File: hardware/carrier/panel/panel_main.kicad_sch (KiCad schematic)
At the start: 23 parts, among them J1 GDEY029T94 FPC, J2 CARRIER, J3 FRONTLIGHT FPC, Q5 AO3400A

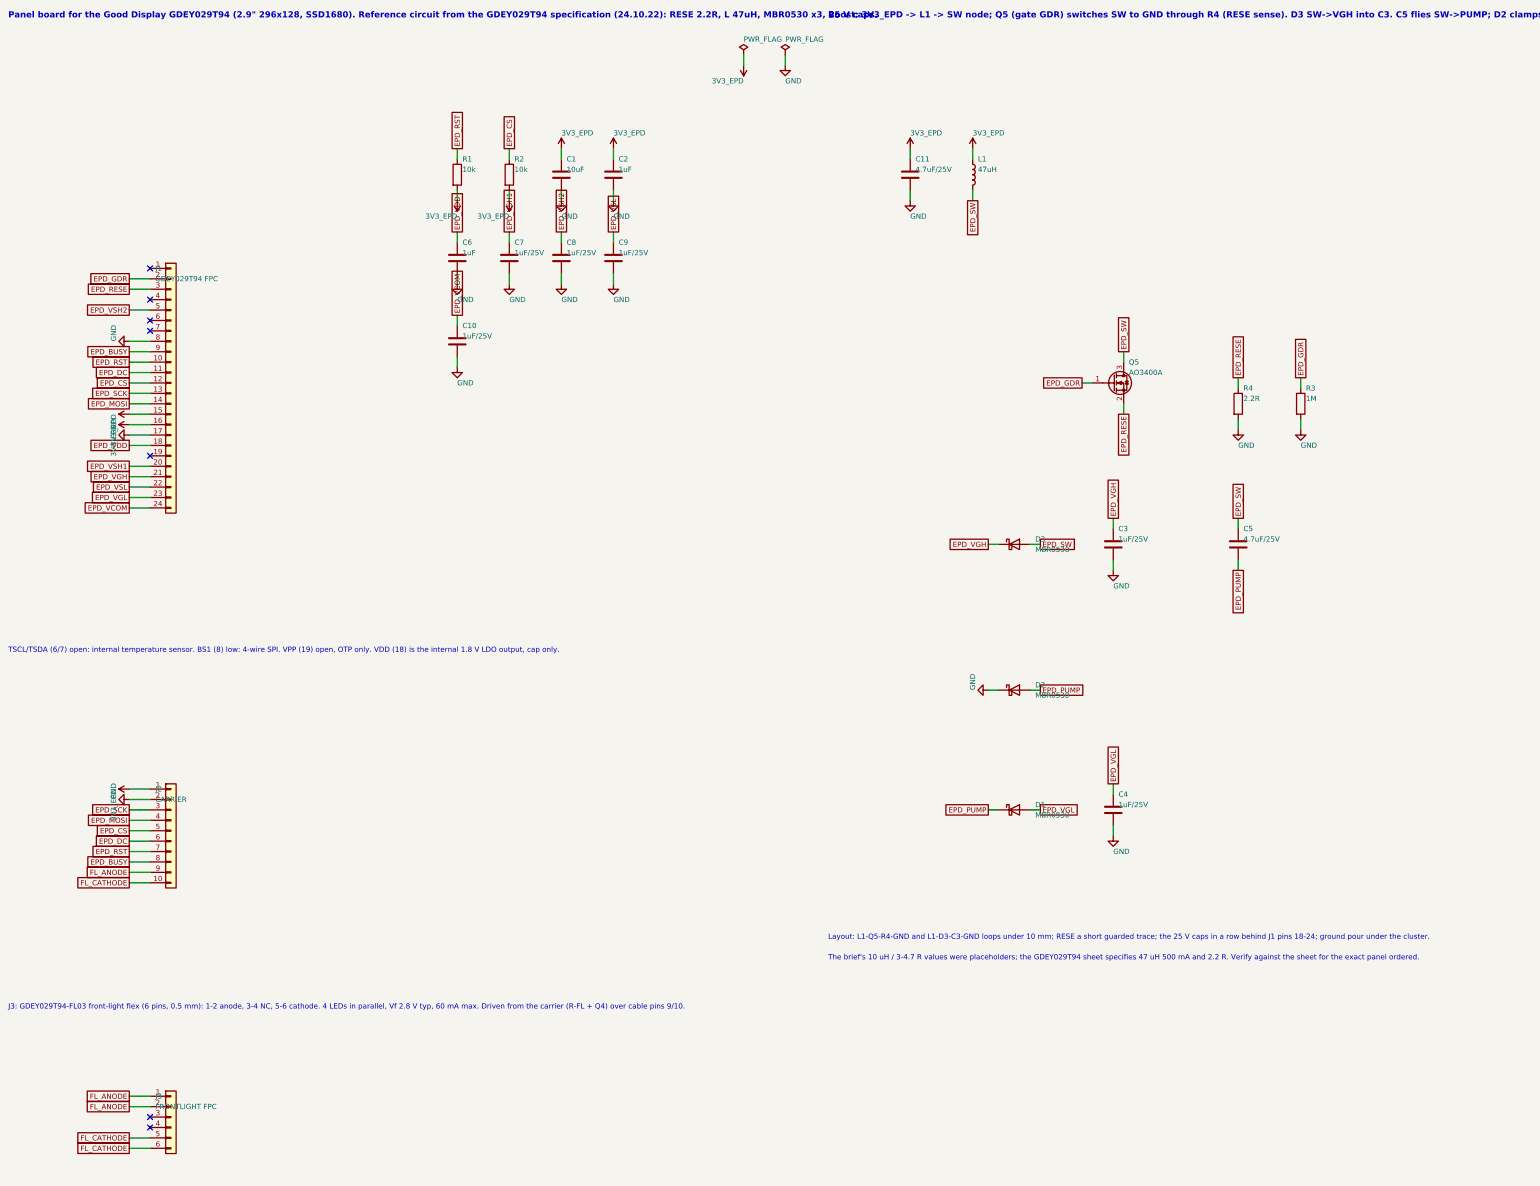
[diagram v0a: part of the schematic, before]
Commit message: Fix some small errors and clean up BOM
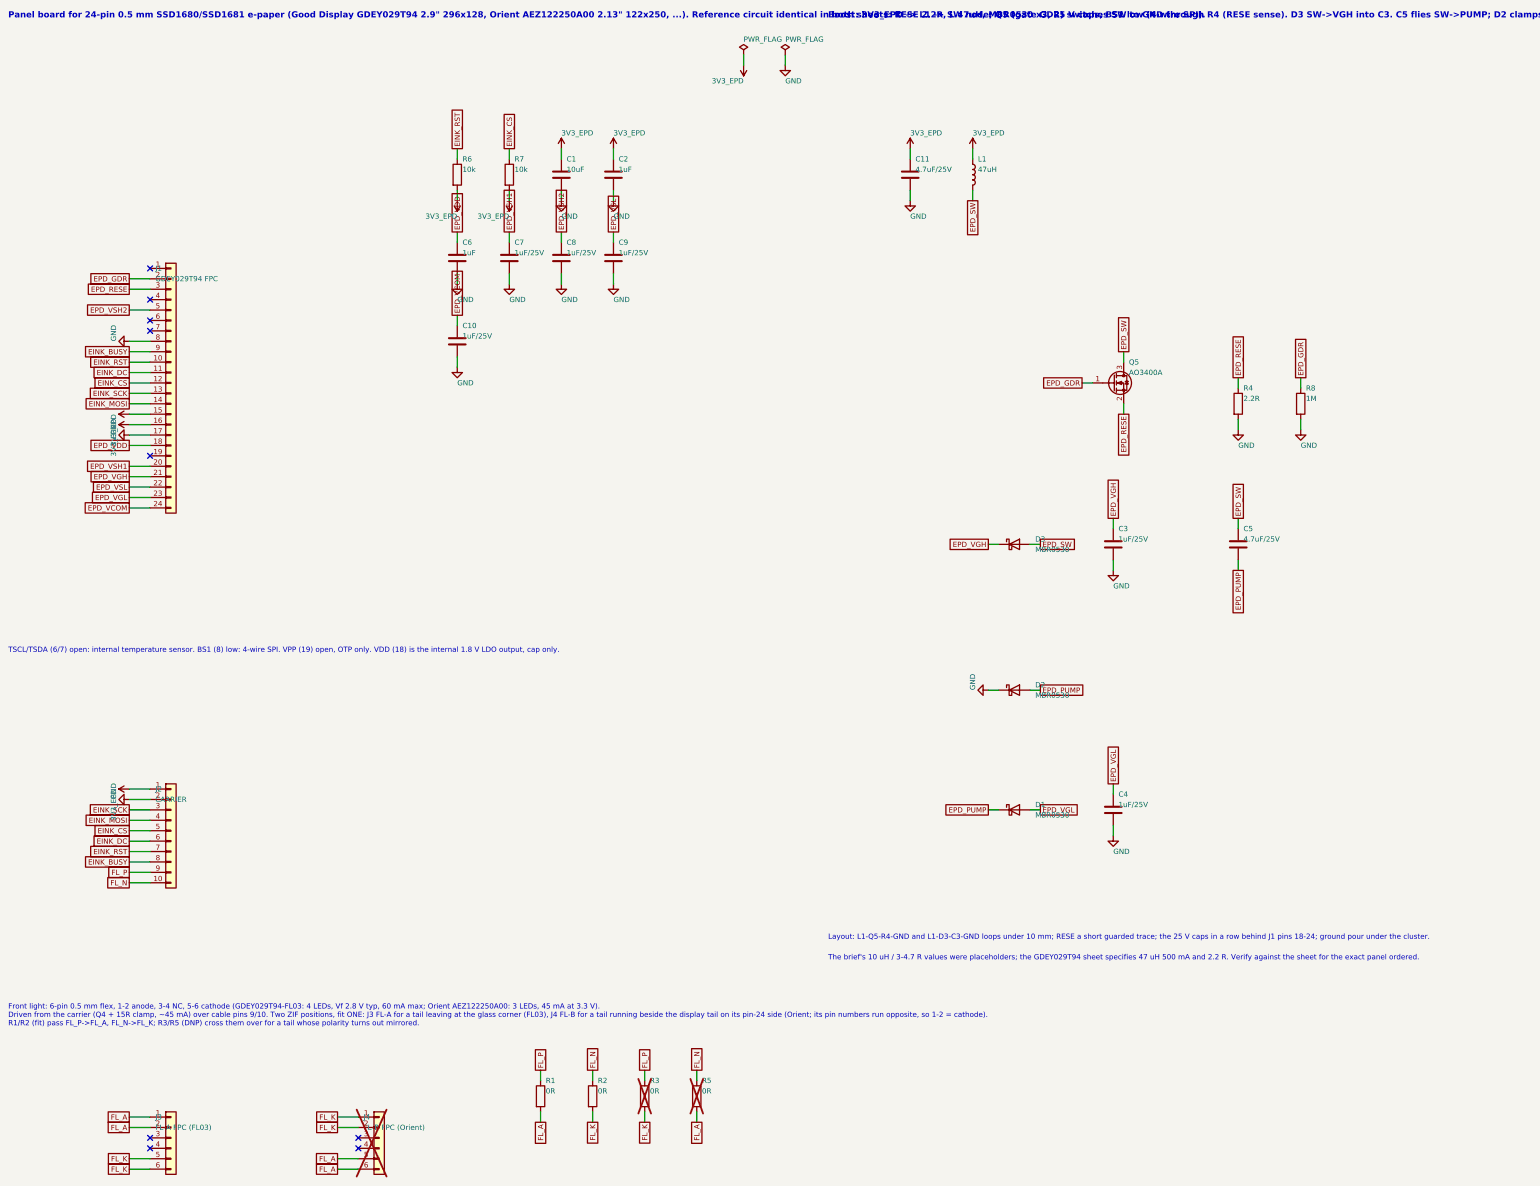
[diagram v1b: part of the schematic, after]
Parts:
- added J4: FL-B FPC (Orient), pager-carrier:Hirose_FH34SRJ-6S-0.5SH_1x06-1MP_P0.50mm_Horizontal, symbol Connector_Generic:Conn_01x06
- added R5: 0R, Resistor_SMD:R_0603_1608Metric, symbol Device:R
- added R6, R7: 10k, Resistor_SMD:R_0603_1608Metric, symbol Device:R
- added R8: 1M, Resistor_SMD:R_0603_1608Metric, symbol Device:R
- J3: value FRONTLIGHT FPC -> FL-A FPC (FL03); Note 1.0 mm high; flex tail is ~30 mm long, folds under with the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 -> 1.0 mm high; GDEY029T94-FL03 corner tail (~30 mm); fit this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
- R1, R2: value 10k -> 0R; LCSC C25804 -> C21189; MPN 0603WAF1002T5E -> 0603WAF0000T5E; Note (none) -> FL straight (fit)
- R3: value 1M -> 0R; DNP (none) -> DNP; LCSC C22935 -> C21189; MPN 0603WAF1004T5E -> 0603WAF0000T5E; Note GDR pull-down -> FL crossover (DNP); now not fitted
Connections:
- net 3V3_EPD: now also R6.2, R7.2; no longer R1.2, R2.2
- net EPD_GDR: now also R8.1; no longer R3.1
- net GND: now also R8.2; no longer R3.2
- net EPD_BUSY renamed EINK_BUSY
- net EPD_CS renamed EINK_CS
- net EINK_CS: now also R7.1; no longer R2.1
- net EPD_DC renamed EINK_DC
- net EPD_MOSI renamed EINK_MOSI
- net EPD_RST renamed EINK_RST
- net EINK_RST: now also R6.1; no longer R1.1
- net EPD_SCK renamed EINK_SCK
- net FL_ANODE renamed FL_A
- net FL_A: now also R1.2, J4.5 (Pin_5), J4.6 (Pin_6), R5.2; no longer J2.9 (Pin_9)
- net FL_CATHODE renamed FL_K
- net FL_K: now also R2.2, R3.2, J4.1 (Pin_1), J4.2 (Pin_2); no longer J2.10 (Pin_10)
- new net FL_N: J2.10 (Pin_10), R2.1, R5.1
- new net FL_P: J2.9 (Pin_9), R1.1, R3.1
- no-connect marks 7 -> 9
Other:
- note added: "Front light: 6-pin 0.5 mm flex, 1-2 anode, 3-4 NC, 5-6 cathode (GDEY029T94-FL03: 4 LEDs, Vf 2.8 V typ, 60 mA max; Orient AEZ122250A00: 3 LEDs, 45 mA at 3.3 V). Driven from the carrier (Q4 + 15R clamp, ~45 mA) over cable pins 9/10. Two ZIF positions, fit ONE: J3 FL-A for a tail leaving at the glass corner (FL03), J4 FL-B for a tail running beside the display tail on its pin-24 side (Orient; its pi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"
- note added: "Panel board for 24-pin 0.5 mm SSD1680/SSD1681 e-paper (Good Display GDEY029T94 2.9" 296x128, Orient AEZ122250A00 2.13" 122x250, ...). Reference circuit identical in both sheets: RESE 2.2R, L 47uH, MBR0530 x3, 25 V caps, BS1 low (4-wire SPI)."
- note removed: "J3: GDEY029T94-FL03 front-light flex (6 pins, 0.5 mm): 1-2 anode, 3-4 NC, 5-6 cathode. 4 LEDs in parallel, Vf 2.8 V typ, 60 mA max. Driven from the carrier (R-FL + Q4) over cable pins 9/10."
- note removed: "Panel board for the Good Display GDEY029T94 (2.9" 296x128, SSD1680). Reference circuit from the GDEY029T94 specification (24.10.22): RESE 2.2R, L 47uH, MBR0530 x3, 25 V caps."
- moved on the sheet: J3, R1, R2

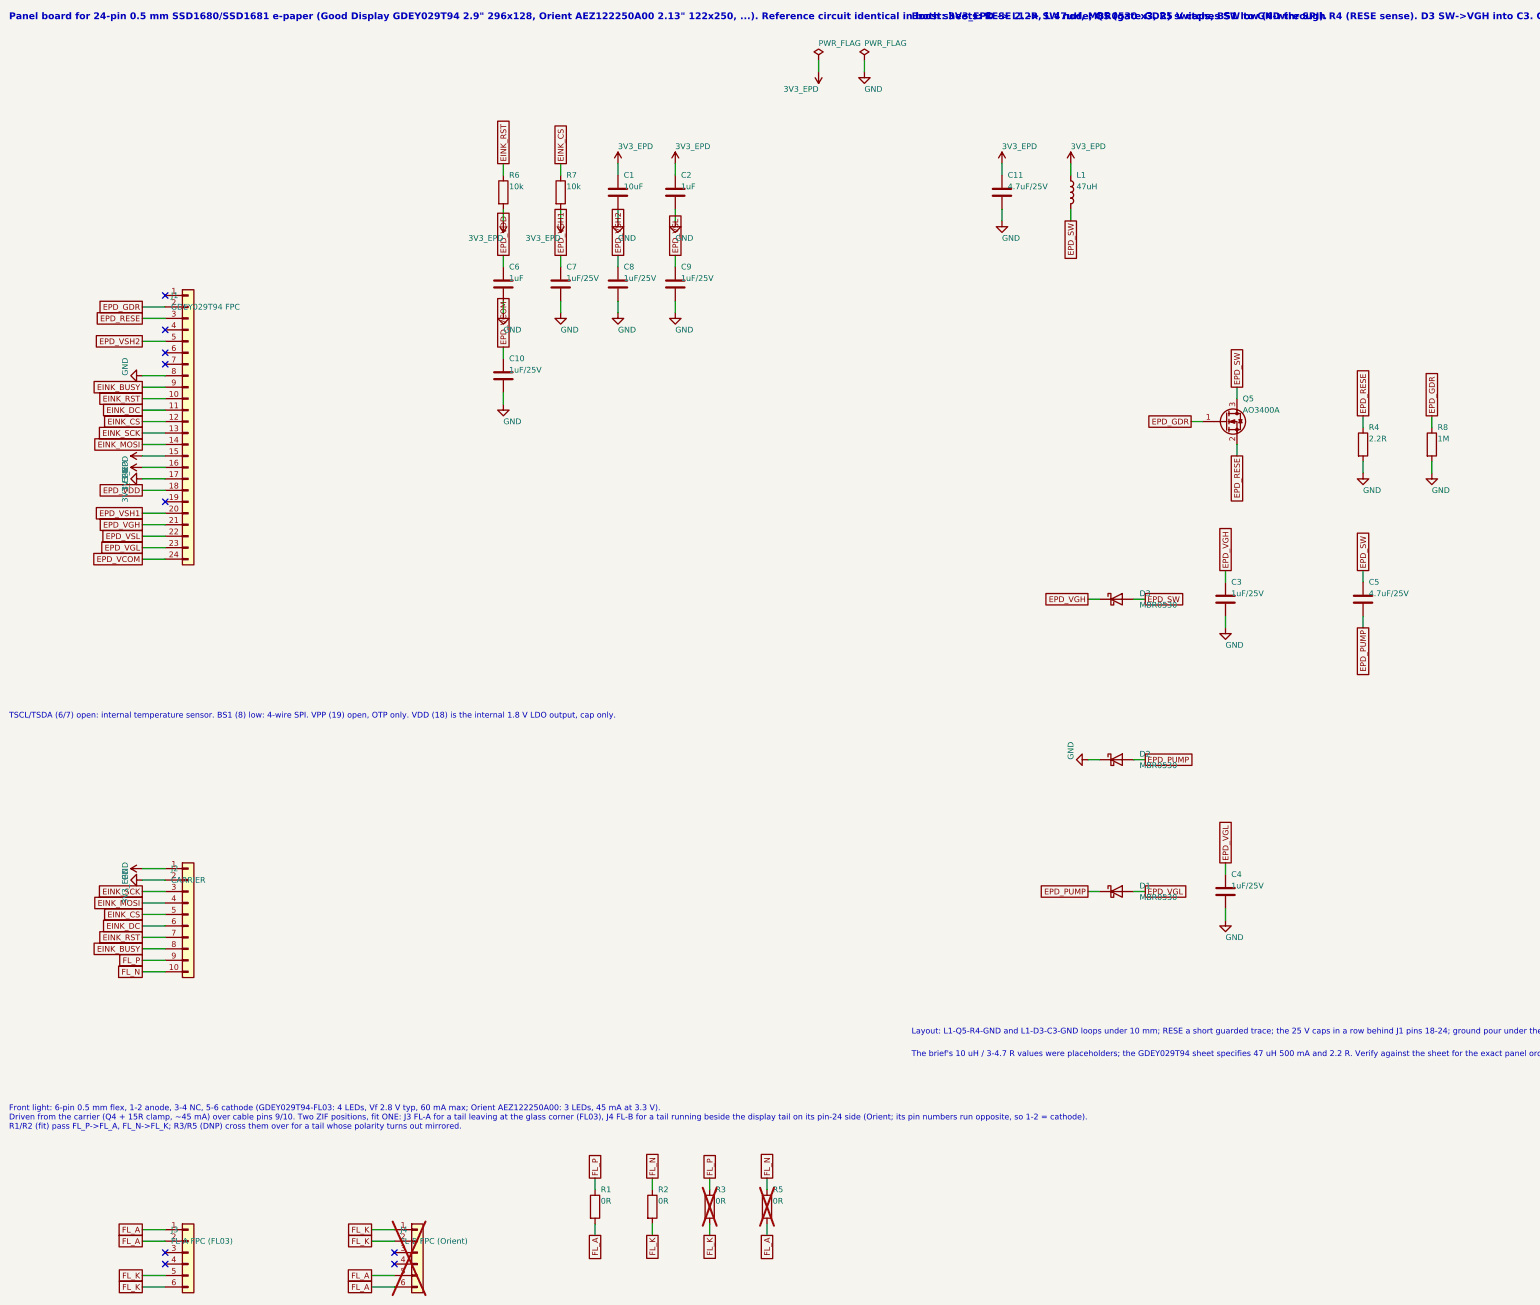
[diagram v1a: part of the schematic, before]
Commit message: Move sheets property to top level
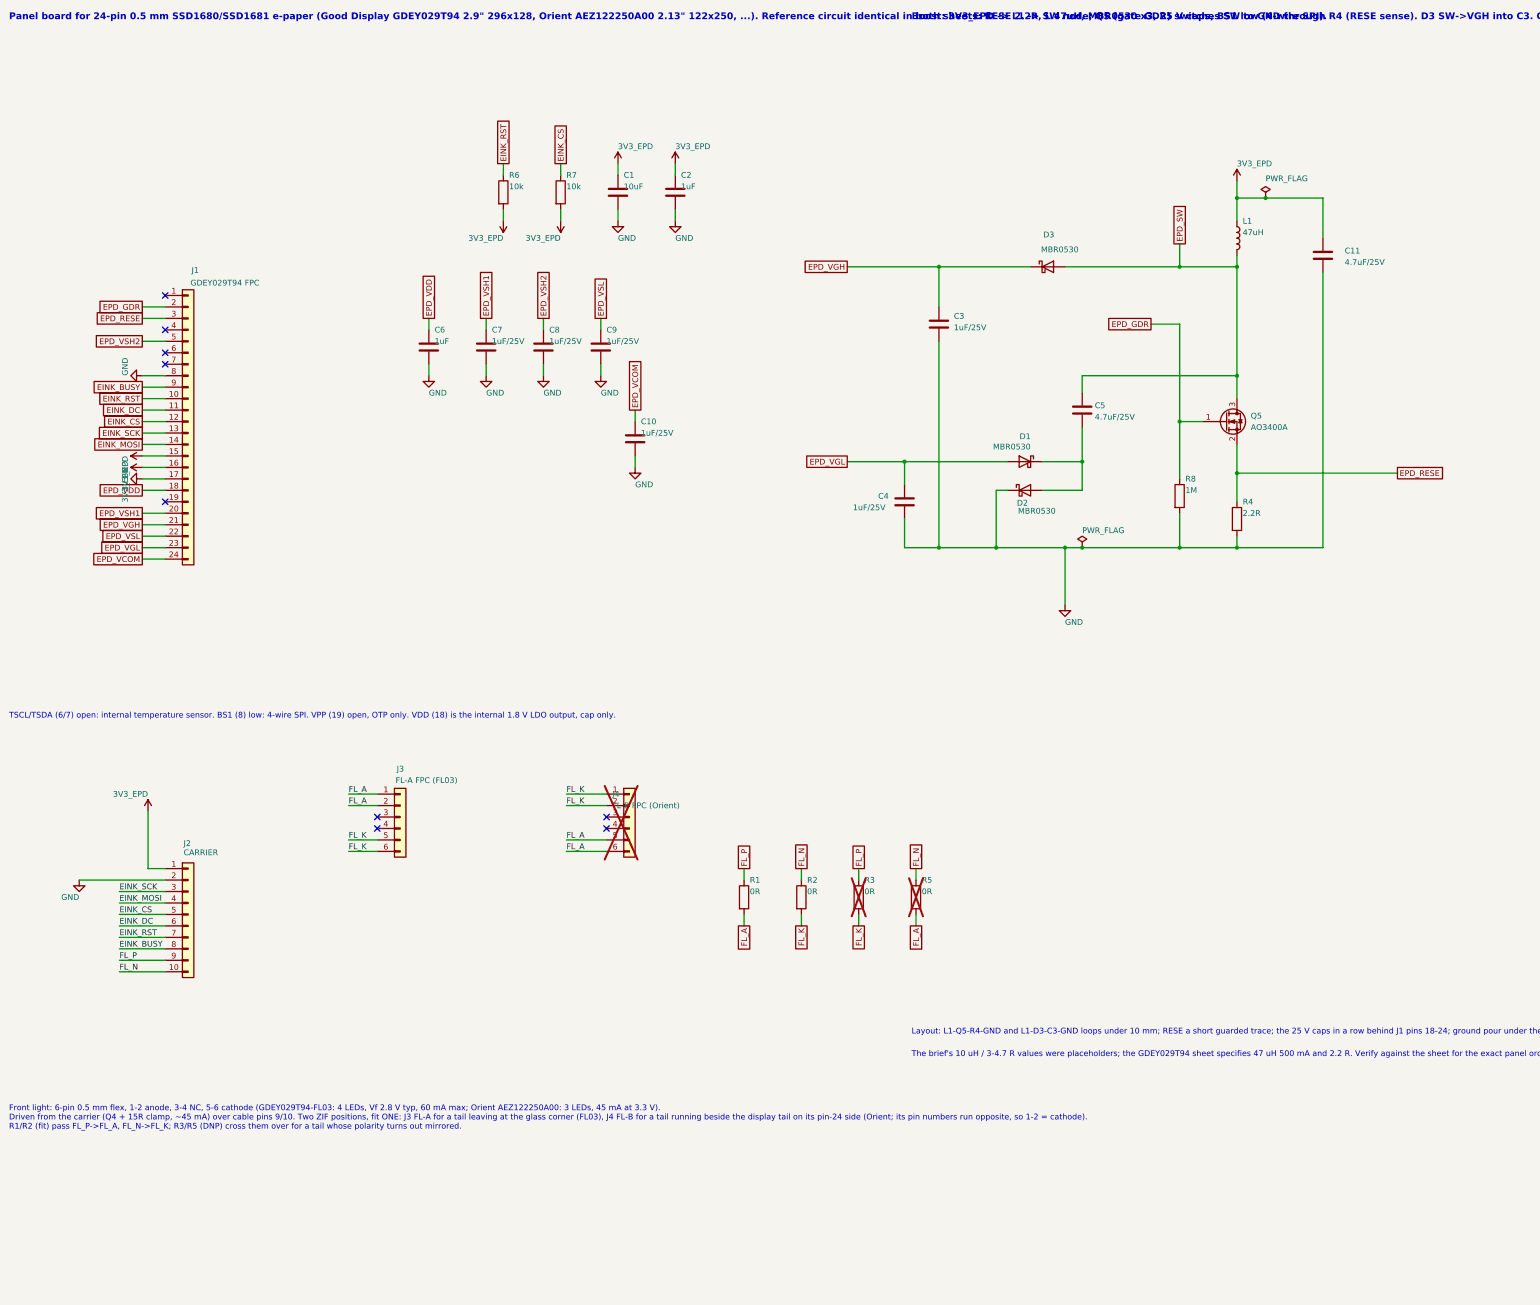
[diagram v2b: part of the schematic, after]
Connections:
- net EPD_PUMP: no longer names the net of C5.2, D1.1 (K), D2.2 (A)
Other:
- moved on the sheet: C10, C11, C3, C4, C5, C6, C7, C8, C9, D1, D2, D3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
